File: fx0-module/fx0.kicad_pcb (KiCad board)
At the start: 2 copper layers, 57.4 x 88.9 mm, 30 parts, among them J1 Line IN, J2 CV IN, J3 Line OUT, J4 CV OUT, U2 Pico, U3 ProMicro

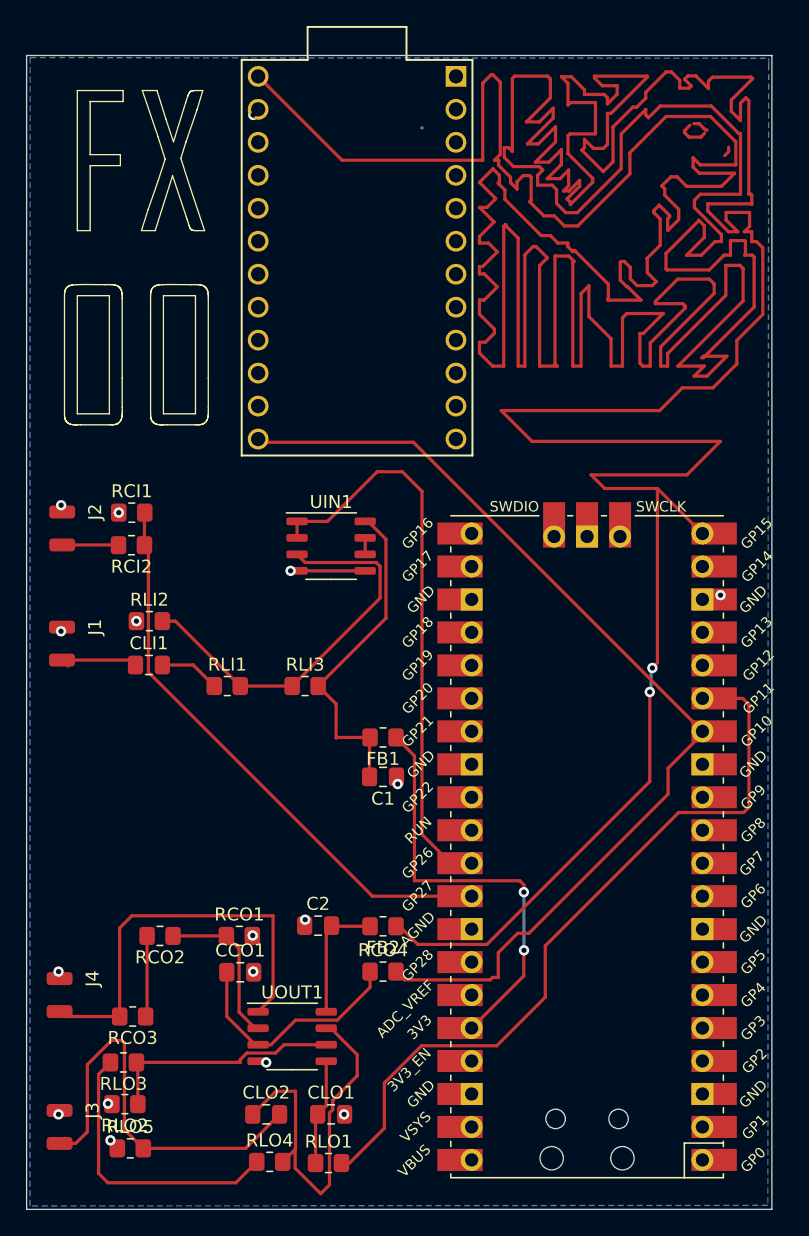
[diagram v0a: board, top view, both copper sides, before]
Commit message: Change value for rc filter
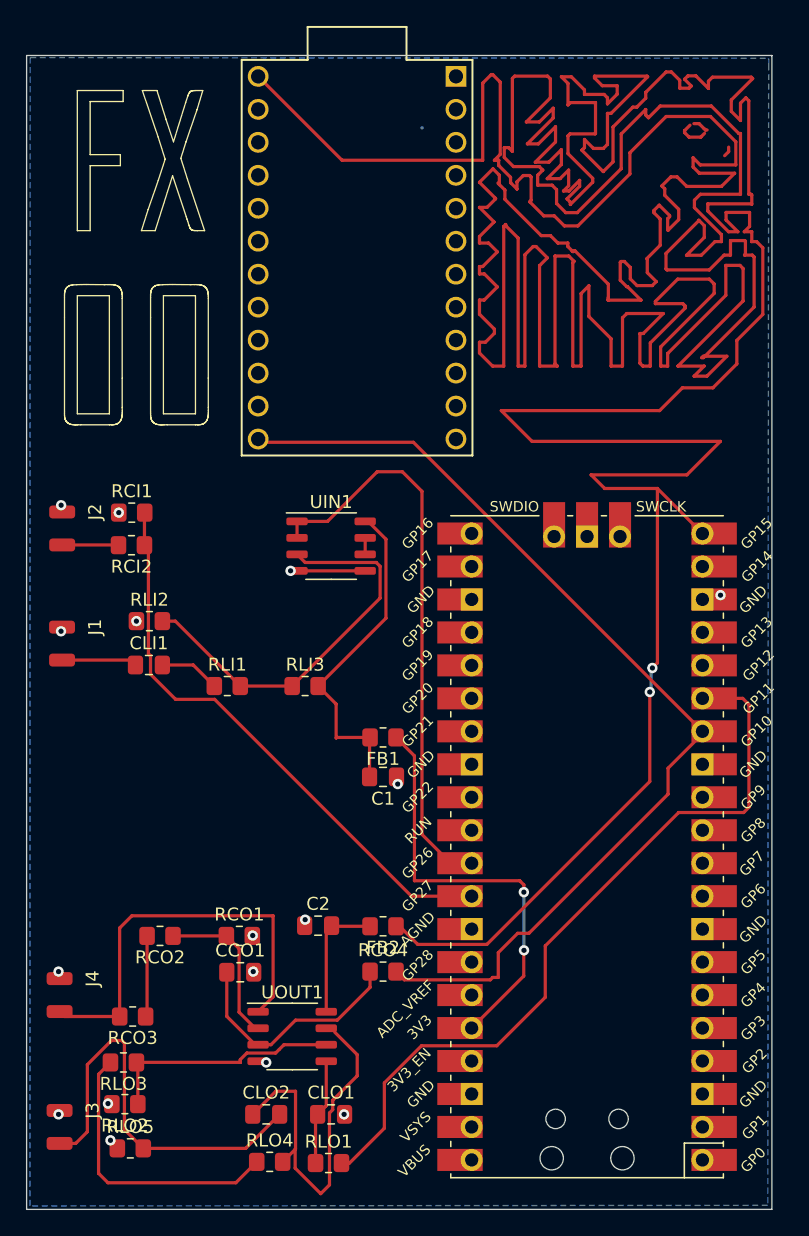
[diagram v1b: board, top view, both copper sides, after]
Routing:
- net Net-(CLI1-Pad1): track 6.47 -> 5.81 mm
- net GND: vias 17 -> 16
